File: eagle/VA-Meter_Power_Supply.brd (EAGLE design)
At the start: 100 x 80 mm, 18 parts, among them IC2 7805TV, T1 2SA1359

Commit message: VA-Meter_Power_Supply.brd 測定部の電源、基板設計図修正、ジャンパをなしに
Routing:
- net V-GND: track 107.7 -> 132.1 mm
- net N$6: track 0.00 -> 4.96 mm
- net 5V: track 66.0 -> 63.5 mm
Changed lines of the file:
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@@
 <layer number="37" name="tTest" color="7" fill="1" visible="no" active="yes"/>
 <layer number="38" name="bTest" color="7" fill="1" visible="no" active="yes"/>
-<layer number="39" name="tKeepout" color="4" fill="11" visible="yes" active="yes"/>
+<layer number="39" name="tKeepout" color="4" fill="11" visible="no" active="yes"/>
 <layer number="40" name="bKeepout" color="1" fill="11" visible="yes" active="yes"/>
 <layer number="41" name="tRestrict" color="4" fill="10" visible="yes" active="yes"/>
@@
 <contactref element="PF2" pad="1"/>
 <contactref element="V-IN" pad="1"/>
-<wire x1="5.207" y1="17.78" x2="10.16" y2="17.79" width="0" layer="19" extent="1-1"/>
+<wire x1="5.207" y1="17.78" x2="10.16" y2="17.78" width="0.4064" layer="16"/>
+<wire x1="10.16" y1="17.78" x2="10.16" y2="17.79" width="0.4064" layer="16"/>
 </signal>
 <signal name="N$7">
@@
 <contactref element="JP1" pad="1"/>
 <contactref element="JP1" pad="2"/>
-<wire x1="27.94" y1="20.32" x2="27.94" y2="17.78" width="0.6096" layer="16"/>
-<wire x1="27.94" y1="17.78" x2="30.48" y2="17.78" width="0.6096" layer="16"/>
 <wire x1="30.48" y1="17.78" x2="33.02" y2="17.78" width="0.6096" layer="16"/>
 <wire x1="33.02" y1="17.78" x2="33.02" y2="12.7" width="0.6096" layer="16"/>
-<wire x1="30.48" y1="17.78" x2="30.48" y2="25.4" width="0.6096" layer="16"/>
+<wire x1="30.48" y1="17.78" x2="30.48" y2="20.32" width="0.6096" layer="16"/>
+<wire x1="30.48" y1="20.32" x2="30.48" y2="25.4" width="0.6096" layer="16"/>
 <wire x1="30.48" y1="25.4" x2="45.72" y2="25.4" width="0.6096" layer="16"/>
 <wire x1="45.72" y1="22.86" x2="45.72" y2="25.4" width="0.6096" layer="16"/>
@@
 <wire x1="45.72" y1="17.78" x2="45.72" y2="22.86" width="0.6096" layer="16"/>
 <wire x1="63.5" y1="25.4" x2="66.04" y2="25.4" width="0.6096" layer="16"/>
+<wire x1="27.94" y1="20.32" x2="30.48" y2="20.32" width="0.6096" layer="16"/>
 </signal>
 <signal name="V-GND">
@@
 <wire x1="33.02" y1="33.02" x2="35.56" y2="33.02" width="0.6096" layer="16"/>
 <wire x1="35.56" y1="33.02" x2="35.56" y2="27.94" width="0.6096" layer="16"/>
-<wire x1="35.56" y1="27.94" x2="25.4" y2="27.94" width="0.6096" layer="16"/>
-<wire x1="25.4" y1="27.94" x2="25.4" y2="20.32" width="0.6096" layer="16"/>
-<wire x1="35.56" y1="17.78" x2="35.56" y2="12.7" width="0.6096" layer="16"/>
-<wire x1="38.1" y1="17.78" x2="35.56" y2="17.78" width="0.6096" layer="16"/>
-<wire x1="35.56" y1="17.78" x2="35.56" y2="10.16" width="0.6096" layer="16"/>
-<wire x1="35.56" y1="10.16" x2="25.4" y2="10.16" width="0.6096" layer="16"/>
-<wire x1="25.4" y1="10.16" x2="25.4" y2="20.32" width="0.6096" layer="16"/>
-<wire x1="50.8" y1="22.86" x2="50.8" y2="15.24" width="0.6096" layer="16"/>
-<wire x1="50.8" y1="15.24" x2="58.42" y2="15.24" width="0.6096" layer="16"/>
 <wire x1="58.42" y1="15.24" x2="58.42" y2="12.7" width="0.6096" layer="16"/>
 <wire x1="63.5" y1="20.32" x2="63.5" y2="15.24" width="0.6096" layer="16"/>
 <wire x1="63.5" y1="15.24" x2="58.42" y2="15.24" width="0.6096" layer="16"/>
 <wire x1="63.5" y1="20.32" x2="66.04" y2="20.32" width="0.6096" layer="16"/>
-<wire x1="38.1" y1="17.78" x2="50.8" y2="22.86" width="0.6096" layer="1"/>
+<wire x1="35.56" y1="27.94" x2="68.58" y2="27.94" width="0.6096" layer="16"/>
+<wire x1="68.58" y1="27.94" x2="68.58" y2="20.32" width="0.6096" layer="16"/>
+<wire x1="68.58" y1="20.32" x2="66.04" y2="20.32" width="0.6096" layer="16"/>
+<wire x1="25.4" y1="20.32" x2="25.4" y2="10.16" width="0.6096" layer="16"/>
+<wire x1="25.4" y1="10.16" x2="35.56" y2="10.16" width="0.6096" layer="16"/>
+<wire x1="35.56" y1="10.16" x2="35.56" y2="12.7" width="0.6096" layer="16"/>
+<wire x1="35.56" y1="27.94" x2="25.4" y2="27.94" width="0.6096" layer="16"/>
+<wire x1="25.4" y1="27.94" x2="25.4" y2="20.32" width="0.6096" layer="16"/>
+<wire x1="35.56" y1="12.7" x2="35.56" y2="17.78" width="0.6096" layer="16"/>
+<wire x1="35.56" y1="17.78" x2="38.1" y2="17.78" width="0.6096" layer="16"/>
+<wire x1="50.8" y1="22.86" x2="50.8" y2="15.24" width="0.6096" layer="16"/>
+<wire x1="50.8" y1="15.24" x2="58.42" y2="15.24" width="0.6096" layer="16"/>
 </signal>
 <signal name="3.3V">

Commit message: VA-Meter_Power_Supply 回路図の電解コンデンサの値を47uFに変更
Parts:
- C2: value 10u -> 47u
- D1: value 1S2 -> 1S4
- moved D1 2.54 mm to (44.5, 22.9)
- moved R11 2.54 mm to (17.8, 34.3)
- moved R8 2.54 mm to (15.2, 34.3)
- moved C3 2.54 mm to (29.2, 20.3)
- moved C7 2.54 mm to (35.6, 17.8), turned to 270 degrees
- moved C8 2.54 mm to (38.1, 30.5)
- moved D2 2.54 mm to (55.9, 22.9)
- moved D3 2.54 mm to (22.9, 35.6)
- moved IC2 2.54 mm to (38.1, 10.2)
- moved JP1 2.54 mm to (62.2, 22.9)
- moved PF1 2.54 mm to (12.7, 27.9)
- moved PF2 2.54 mm to (12.7, 15.2)
- moved R2 2.54 mm to (54.6, 17.8)
- moved R7 2.54 mm to (20.3, 34.3)
- moved T1 2.54 mm to (38.1, 36.8)
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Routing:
- net 3.3V: track 15.2 -> 10.2 mm
- net 5V: track 63.5 -> 61.0 mm
- net N$6: track 4.96 -> 7.50 mm
- net GND: track 38.0 -> 40.5 mm
- net N$7: track 7.50 -> 10.0 mm
- net V-GND: track 132.1 -> 129.6 mm
- net +15V: track 71.1 -> 68.6 mm

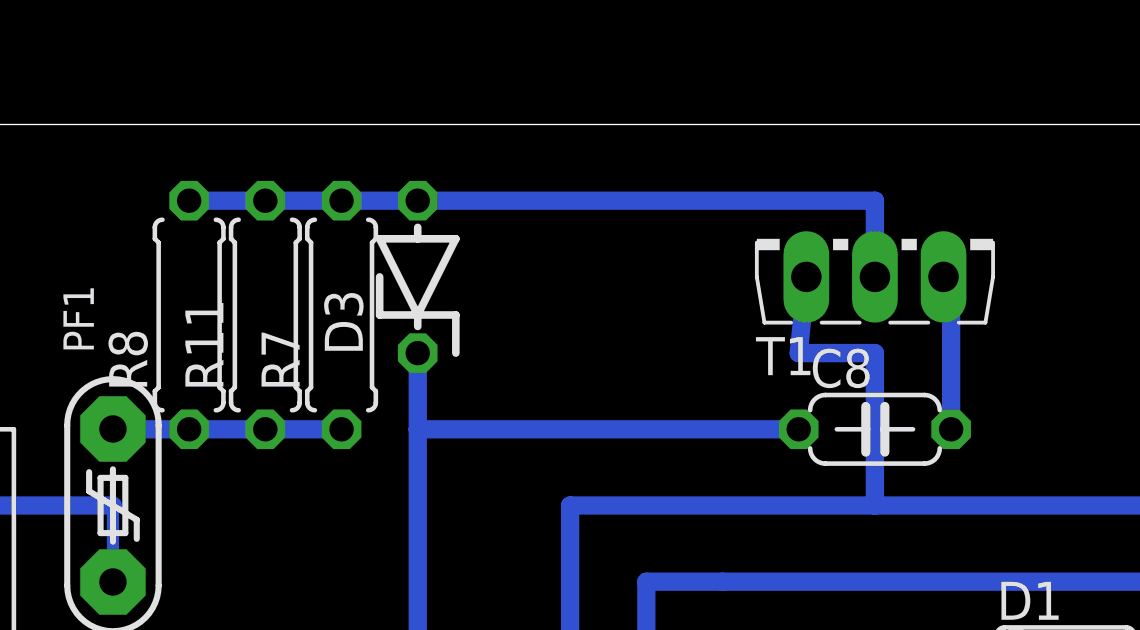
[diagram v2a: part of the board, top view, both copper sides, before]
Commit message: VA-Meter_Power_Supply 2SA1359の定電圧源の回路が間違っていたので修正
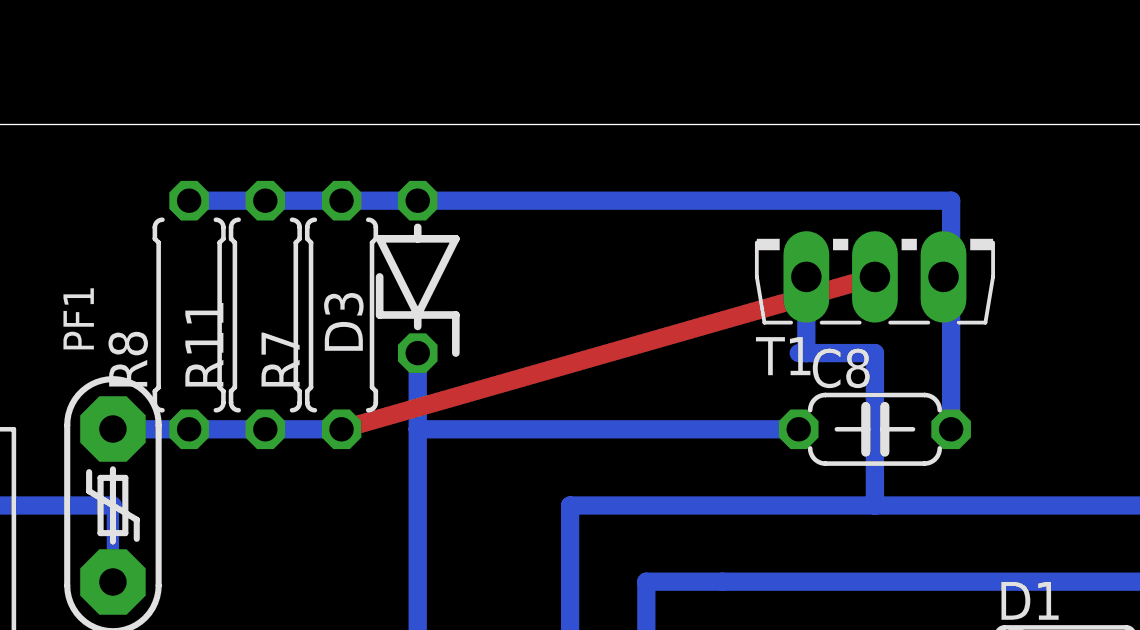
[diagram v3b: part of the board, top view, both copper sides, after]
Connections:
- removed net N$1: D3.A, R11.2, R7.2, R8.2, T1.2
- removed net N$5: C8.2, T1.3
- new net N$2: C8.2, D3.A, R11.2, R7.2, R8.2, T1.3
- net -15V: now also T1.2
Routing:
- net N$2: track 0.00 -> 33.4 mm
- net N$1: track 25.4 -> 0.00 mm
- net -15V: track 7.63 -> 26.1 mm
- net N$5: track 5.19 -> 0.00 mm
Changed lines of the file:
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@@
 <layer number="37" name="tTest" color="7" fill="1" visible="no" active="yes"/>
 <layer number="38" name="bTest" color="7" fill="1" visible="no" active="yes"/>
-<layer number="39" name="tKeepout" color="4" fill="11" visible="yes" active="yes"/>
+<layer number="39" name="tKeepout" color="4" fill="11" visible="no" active="yes"/>
 <layer number="40" name="bKeepout" color="1" fill="11" visible="yes" active="yes"/>
 <layer number="41" name="tRestrict" color="4" fill="10" visible="yes" active="yes"/>
@@
 <wire x1="15.24" y1="30.48" x2="17.78" y2="30.48" width="0.6096" layer="16"/>
 <wire x1="17.78" y1="30.48" x2="20.32" y2="30.48" width="0.6096" layer="16"/>
-</signal>
-<signal name="N$1">
-<contactref element="R8" pad="2"/>
-<contactref element="D3" pad="A"/>
 <contactref element="T1" pad="2"/>
-<contactref element="R11" pad="2"/>
-<contactref element="R7" pad="2"/>
-<wire x1="38.1" y1="35.56" x2="38.1" y2="38.1" width="0.6096" layer="16"/>
-<wire x1="38.1" y1="38.1" x2="22.86" y2="38.1" width="0.6096" layer="16"/>
-<wire x1="22.86" y1="38.1" x2="20.32" y2="38.1" width="0.6096" layer="16"/>
-<wire x1="20.32" y1="38.1" x2="17.78" y2="38.1" width="0.6096" layer="16"/>
-<wire x1="17.78" y1="38.1" x2="15.24" y2="38.1" width="0.6096" layer="16"/>
-</signal>
-<signal name="N$5">
-<contactref element="T1" pad="3"/>
-<contactref element="C8" pad="2"/>
-<wire x1="40.64" y1="30.48" x2="40.64" y2="35.306" width="0.6096" layer="16"/>
-<wire x1="40.64" y1="35.306" x2="40.386" y2="35.56" width="0.6096" layer="16"/>
+<wire x1="20.32" y1="30.48" x2="38.1" y2="35.56" width="0.6096" layer="1"/>
 </signal>
 <signal name="N$6">
@@
 <contactref element="C6" pad="1"/>
 <contactref element="C7" pad="1"/>
-<contactref element="T1" pad="1"/>
 <contactref element="D2" pad="A"/>
 <contactref element="JP1" pad="5"/>
 <contactref element="JP1" pad="6"/>
-<wire x1="35.814" y1="35.56" x2="35.56" y2="33.02" width="0.6096" layer="16"/>
-<wire x1="35.56" y1="33.02" x2="38.1" y2="33.02" width="0.6096" layer="16"/>
+<wire x1="35.814" y1="33.02" x2="38.1" y2="33.02" width="0.6096" layer="16"/>
 <wire x1="38.1" y1="33.02" x2="38.1" y2="27.94" width="0.6096" layer="16"/>
 <wire x1="58.42" y1="15.24" x2="58.42" y2="12.7" width="0.6096" layer="16"/>
@@
 <wire x1="35.56" y1="20.32" x2="38.1" y2="20.32" width="0.6096" layer="16"/>
 <wire x1="38.1" y1="20.32" x2="38.1" y2="12.7" width="0.6096" layer="16"/>
+<contactref element="T1" pad="1"/>
+<wire x1="35.56" y1="33.02" x2="35.814" y2="33.02" width="0.6096" layer="16"/>
+<wire x1="35.814" y1="33.02" x2="35.814" y2="35.56" width="0.6096" layer="16"/>
 </signal>
 <signal name="3.3V">
@@
 <wire x1="60.96" y1="22.86" x2="63.5" y2="22.86" width="0.6096" layer="16"/>
 </signal>
+<signal name="N$2">
+<contactref element="R7" pad="2"/>
+<contactref element="R8" pad="2"/>
+<contactref element="D3" pad="A"/>
+<contactref element="T1" pad="3"/>
+<contactref element="C8" pad="2"/>
+<contactref element="R11" pad="2"/>
+<wire x1="40.64" y1="38.1" x2="22.86" y2="38.1" width="0.6096" layer="16"/>
+<wire x1="40.64" y1="30.48" x2="40.64" y2="35.306" width="0.6096" layer="16"/>
+<wire x1="40.64" y1="35.306" x2="40.386" y2="35.56" width="0.6096" layer="16"/>
+<wire x1="40.386" y1="35.56" x2="40.64" y2="35.56" width="0.6096" layer="16"/>
+<wire x1="40.64" y1="35.56" x2="40.64" y2="38.1" width="0.6096" layer="16"/>
+<wire x1="15.24" y1="38.1" x2="17.78" y2="38.1" width="0.6096" layer="16"/>
+<wire x1="17.78" y1="38.1" x2="20.32" y2="38.1" width="0.6096" layer="16"/>
+<wire x1="20.32" y1="38.1" x2="22.86" y2="38.1" width="0.6096" layer="16"/>
+</signal>
 </signals>

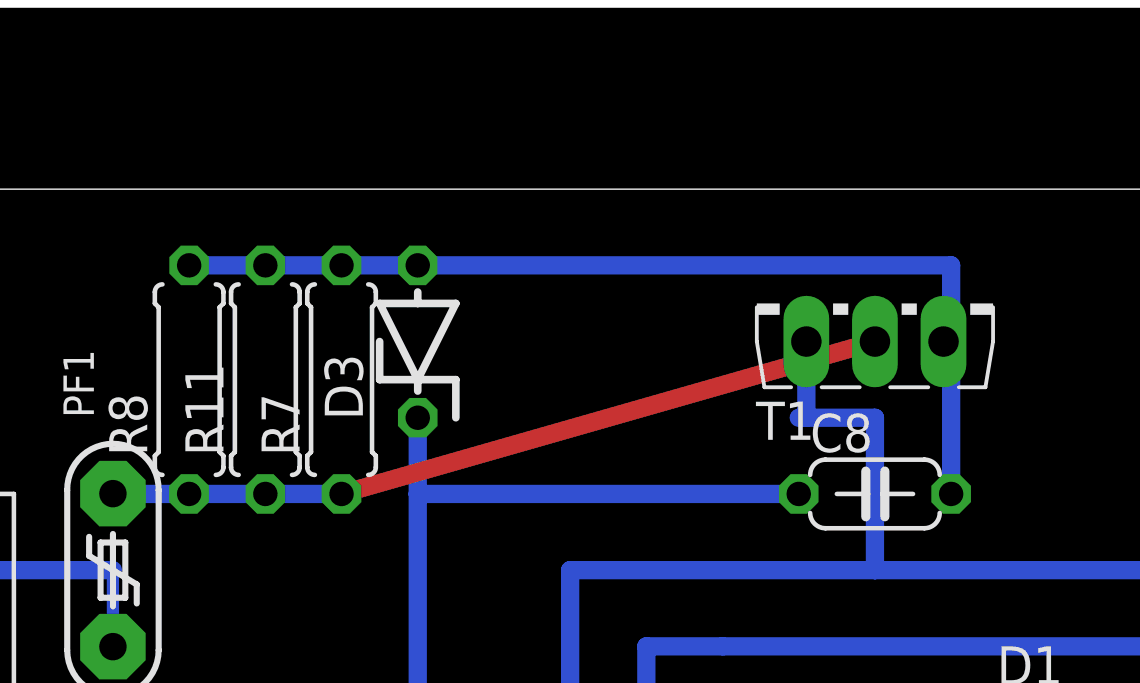
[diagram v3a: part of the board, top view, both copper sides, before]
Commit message: VA-Meter_Power_Supply 基板図をジャンパを使わないように修正
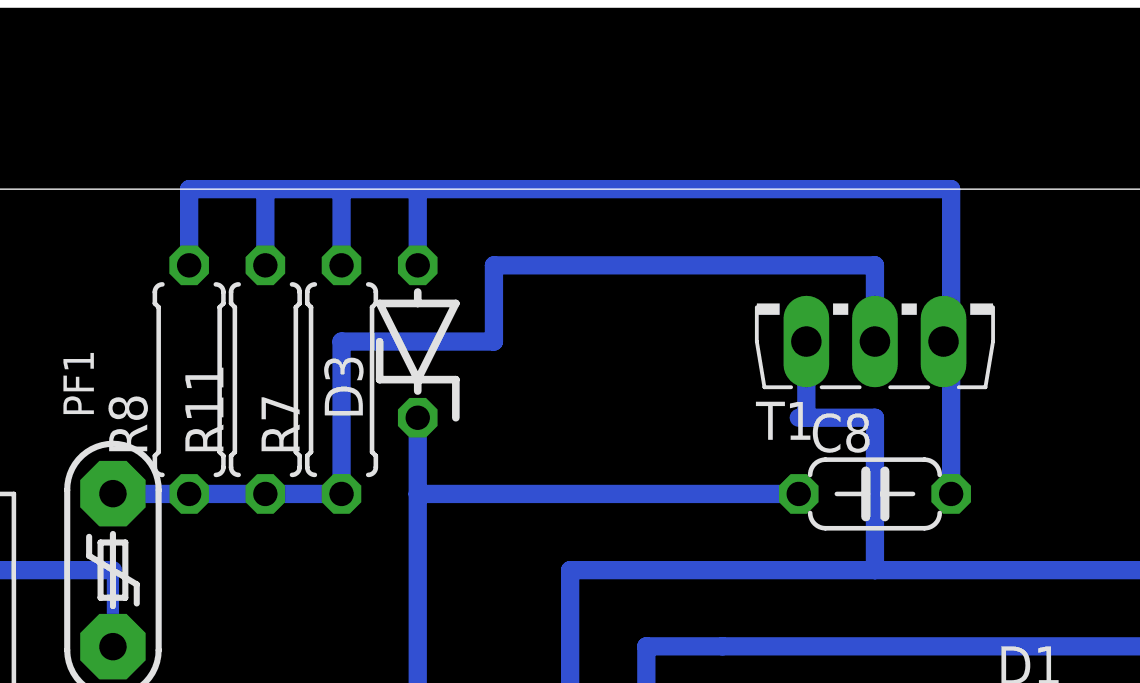
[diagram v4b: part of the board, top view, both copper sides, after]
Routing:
- net N$2: track 33.4 -> 46.1 mm
- net -15V: track 26.1 -> 35.6 mm
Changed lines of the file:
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@@
 <layer number="37" name="tTest" color="7" fill="1" visible="no" active="yes"/>
 <layer number="38" name="bTest" color="7" fill="1" visible="no" active="yes"/>
-<layer number="39" name="tKeepout" color="4" fill="11" visible="no" active="yes"/>
+<layer number="39" name="tKeepout" color="4" fill="11" visible="yes" active="yes"/>
 <layer number="40" name="bKeepout" color="1" fill="11" visible="yes" active="yes"/>
 <layer number="41" name="tRestrict" color="4" fill="10" visible="yes" active="yes"/>
@@
 <layer number="98" name="Guide" color="6" fill="1" visible="no" active="no"/>
 <layer number="99" name="SpiceOrder" color="5" fill="1" visible="no" active="no"/>
-<layer number="100" name="Mesh" color="7" fill="1" visible="no" active="yes"/>
+<layer number="100" name="Mesh" color="7" fill="1" visible="yes" active="yes"/>
 </layers>
 <board>
@@
 <wire x1="17.78" y1="30.48" x2="20.32" y2="30.48" width="0.6096" layer="16"/>
 <contactref element="T1" pad="2"/>
-<wire x1="20.32" y1="30.48" x2="38.1" y2="35.56" width="0.6096" layer="1"/>
+<wire x1="20.32" y1="30.48" x2="20.32" y2="35.56" width="0.6096" layer="16"/>
+<wire x1="20.32" y1="35.56" x2="25.4" y2="35.56" width="0.6096" layer="16"/>
+<wire x1="25.4" y1="35.56" x2="25.4" y2="38.1" width="0.6096" layer="16"/>
+<wire x1="25.4" y1="38.1" x2="38.1" y2="38.1" width="0.6096" layer="16"/>
+<wire x1="38.1" y1="38.1" x2="38.1" y2="35.56" width="0.6096" layer="16"/>
 </signal>
 <signal name="N$6">
@@
 <contactref element="C8" pad="2"/>
 <contactref element="R11" pad="2"/>
-<wire x1="40.64" y1="38.1" x2="22.86" y2="38.1" width="0.6096" layer="16"/>
 <wire x1="40.64" y1="30.48" x2="40.64" y2="35.306" width="0.6096" layer="16"/>
 <wire x1="40.64" y1="35.306" x2="40.386" y2="35.56" width="0.6096" layer="16"/>
 <wire x1="40.386" y1="35.56" x2="40.64" y2="35.56" width="0.6096" layer="16"/>
-<wire x1="40.64" y1="35.56" x2="40.64" y2="38.1" width="0.6096" layer="16"/>
-<wire x1="15.24" y1="38.1" x2="17.78" y2="38.1" width="0.6096" layer="16"/>
-<wire x1="17.78" y1="38.1" x2="20.32" y2="38.1" width="0.6096" layer="16"/>
-<wire x1="20.32" y1="38.1" x2="22.86" y2="38.1" width="0.6096" layer="16"/>
+<wire x1="40.64" y1="35.56" x2="40.64" y2="40.64" width="0.6096" layer="16"/>
+<wire x1="40.64" y1="40.64" x2="22.86" y2="40.64" width="0.6096" layer="16"/>
+<wire x1="22.86" y1="40.64" x2="20.32" y2="40.64" width="0.6096" layer="16"/>
+<wire x1="20.32" y1="40.64" x2="17.78" y2="40.64" width="0.6096" layer="16"/>
+<wire x1="17.78" y1="40.64" x2="15.24" y2="40.64" width="0.6096" layer="16"/>
+<wire x1="15.24" y1="40.64" x2="15.24" y2="38.1" width="0.6096" layer="16"/>
+<wire x1="17.78" y1="38.1" x2="17.78" y2="40.64" width="0.6096" layer="16"/>
+<wire x1="20.32" y1="38.1" x2="20.32" y2="40.64" width="0.6096" layer="16"/>
+<wire x1="22.86" y1="38.1" x2="22.86" y2="40.64" width="0.6096" layer="16"/>
 </signal>
 </signals>
